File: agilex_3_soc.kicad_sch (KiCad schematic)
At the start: 7 parts, among them J1 Conn_01x14, J2 Conn_02x03_Odd_Even, J3 Conn_02x19_Odd_Even, J4 Conn_01x03, J5 Conn_01x03, J8 Conn_01x05, Y1 ASDMB-25MHz

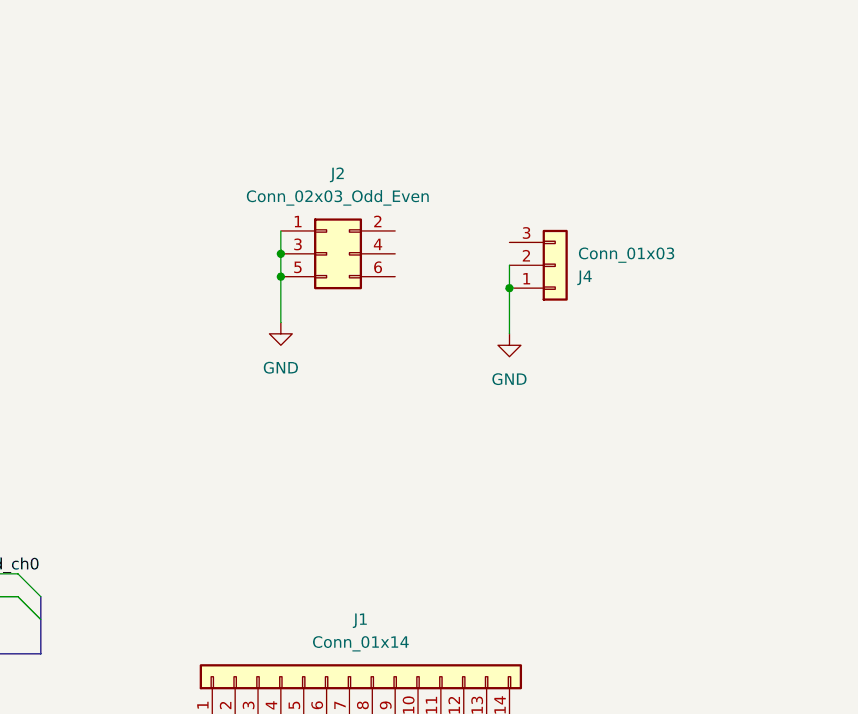
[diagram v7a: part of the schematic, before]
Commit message: even more power supply routing
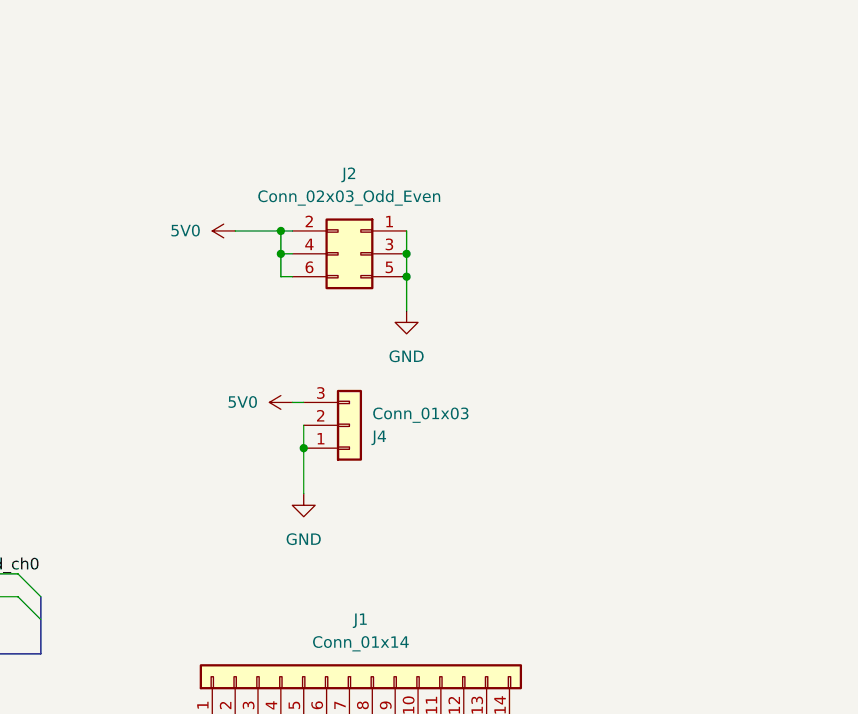
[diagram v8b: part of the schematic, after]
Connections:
- net 5V0: now reaches J2.2 (Pin_2)
- net 5V0: now also J2.4 (Pin_4), J2.6 (Pin_6), J4.3 (Pin_3)
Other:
- moved on the sheet: J2, J4
